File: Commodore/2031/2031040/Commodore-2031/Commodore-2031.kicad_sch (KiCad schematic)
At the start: 11 parts

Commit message: Capture sheet 3
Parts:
- removed UA3, UJ5, UL6: 74LS04, symbol 74xx:74LS04
- removed UB1: 74LS14, symbol 74xx:74LS14
- removed UC1: 7406, symbol 74xx:74LS06
- removed UK6: 74LS10, symbol 74xx:74LS10
- removed UL2: 74LS133, symbol 74xx:74LS133
- removed UM2: 74LS02, symbol 74xx:74LS02
- removed UM3: 74LS74, symbol 74xx:74LS74
- removed UM6: 74LS00, symbol 74xx:74LS00
- removed UP2: 74LS86, symbol 74xx:74LS86
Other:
- added sheet CPUMemoryPowerClock (Sheet3-CPUMemoryPowerClock.kicad_sch)

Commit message: Capture sheet 4
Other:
- added sheet StepperMotorRWAmplifier (Sheet4-StepperMotorRWAmplifier.kicad_sch)
- sheet CPUMemoryPowerClock ports: added 16MHZ; removed 16MHz

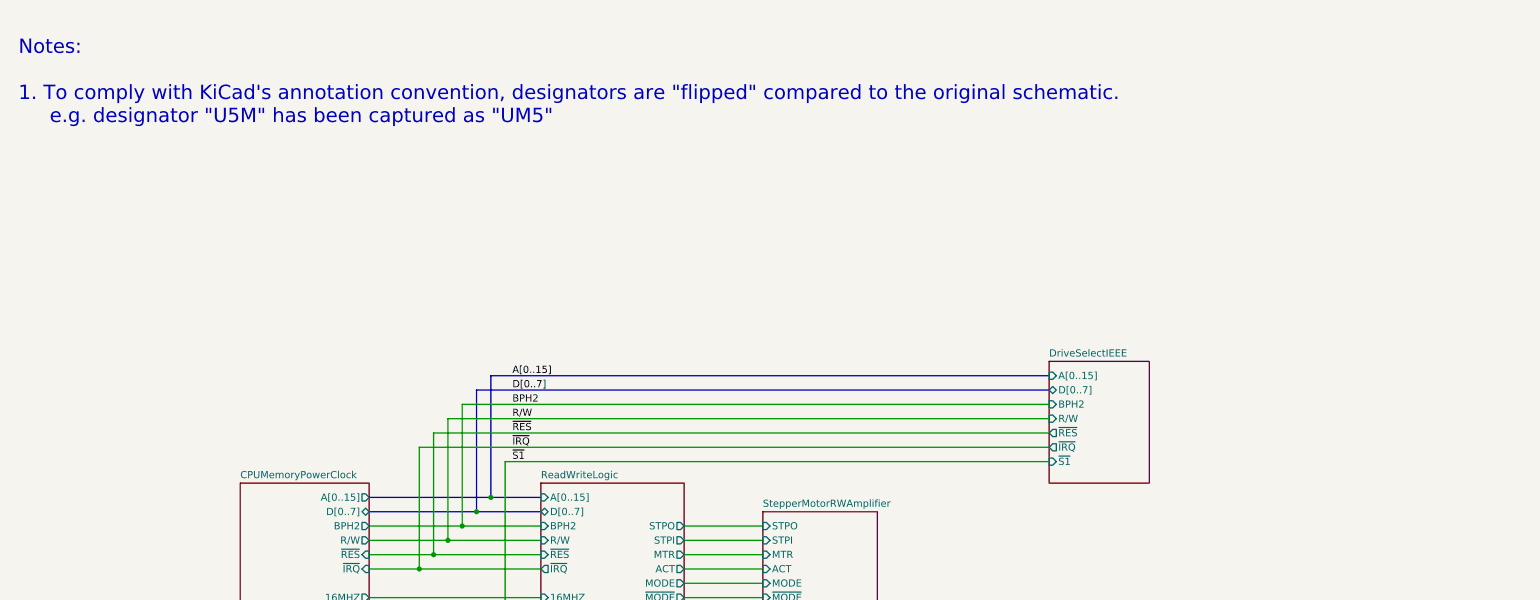
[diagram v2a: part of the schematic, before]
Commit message: Work towards ERC
- Add power flags
- Try to make sense of ground symbols
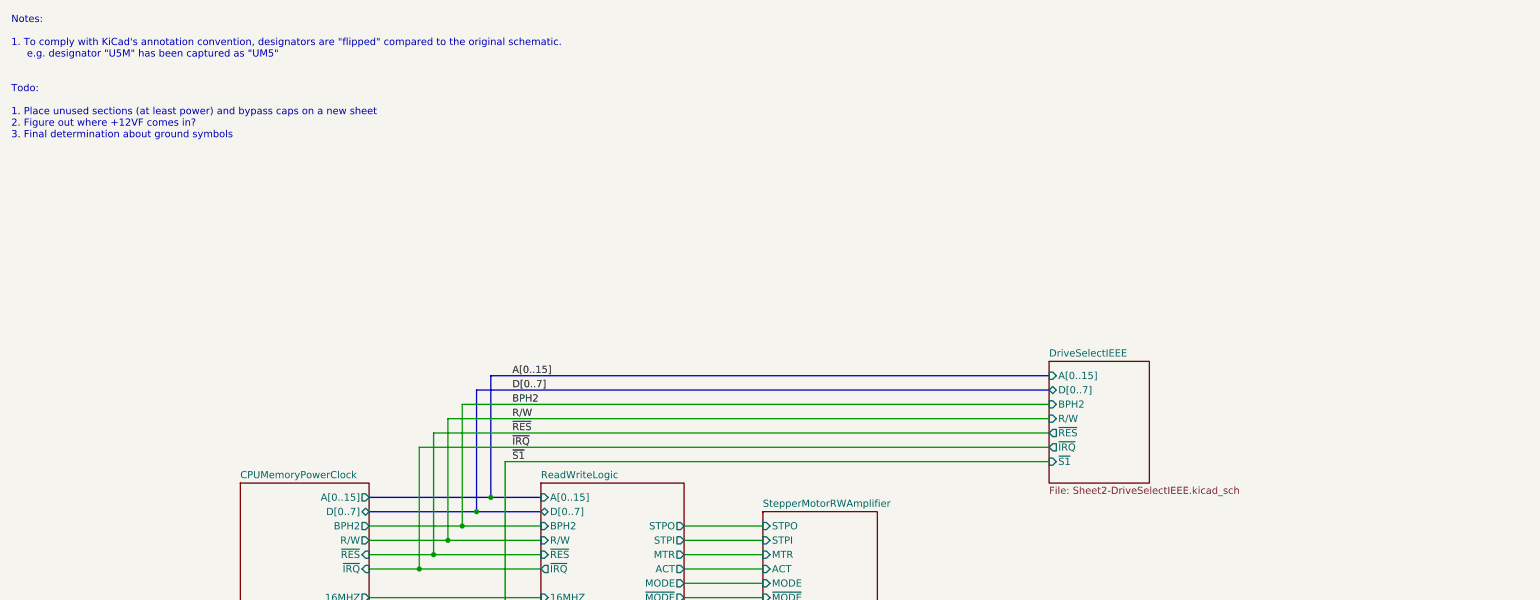
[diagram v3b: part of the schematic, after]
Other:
- note added: "Notes: 1. To comply with KiCad's annotation convention, designators are "flipped" compared to the original schematic. e.g. designator "U5M" has been captured as "UM5" Todo: 1. Place unused sections (at least power) and bypass caps on a new sheet 2. Figure out where +12VF comes in? 3. Final determination about ground symbols"
- note removed: "Notes: 1. To comply with KiCad's annotation convention, designators are "flipped" compared to the original schematic. e.g. designator "U5M" has been captured as "UM5""
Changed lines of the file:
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@@
     (stroke (width 0) (type default))
   )
-  (text "Notes:\n\n1. To comply with KiCad's annotation convention, designators are \"flipped\" compared to the original schematic.\n     e.g. designator \"U5M\" has been captured as \"UM5\""
-    (at 19.05 36.83 0)
-    (effects (font (size 2.54 2.54)) (justify left bottom))
+  (text "Notes:\n\n1. To comply with KiCad's annotation convention, designators are \"flipped\" compared to the original schematic.\n     e.g. designator \"U5M\" has been captured as \"UM5\"\n\n\nTodo:\n\n1. Place unused sections (at least power) and bypass caps on a new sheet\n2. Figure out where +12VF comes in?\n3. Final determination about ground symbols"
+    (at 17.78 39.37 0)
+    (effects (font (size 1.27 1.27)) (justify left bottom))
   )
   (label "A[0..15]" (at 106.68 81.28 0) (fields_autoplaced)
@@
     )
     (property "Sheetfile" "Sheet2-DriveSelectIEEE.kicad_sch" (at 201.93 100.9146 0)
-      (effects (font (size 1.27 1.27)) (justify left top) hide)
+      (effects (font (size 1.27 1.27)) (justify left top))
     )
     (pin "~{IRQ}" output (at 201.93 93.98 180)

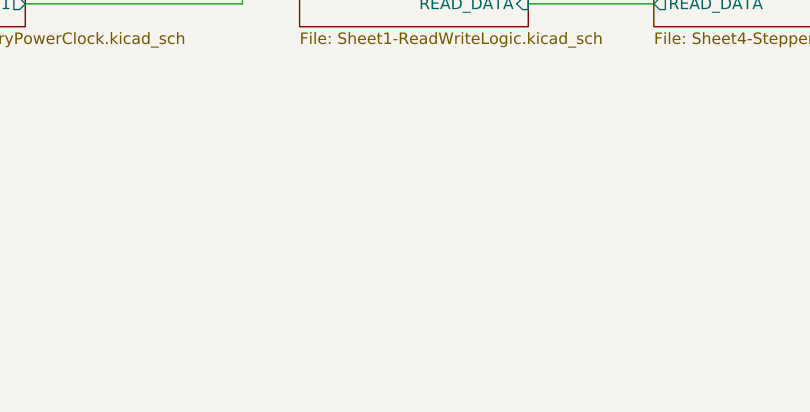
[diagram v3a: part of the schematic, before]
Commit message: Place capacitors and power units
Almost an error-free ERC!
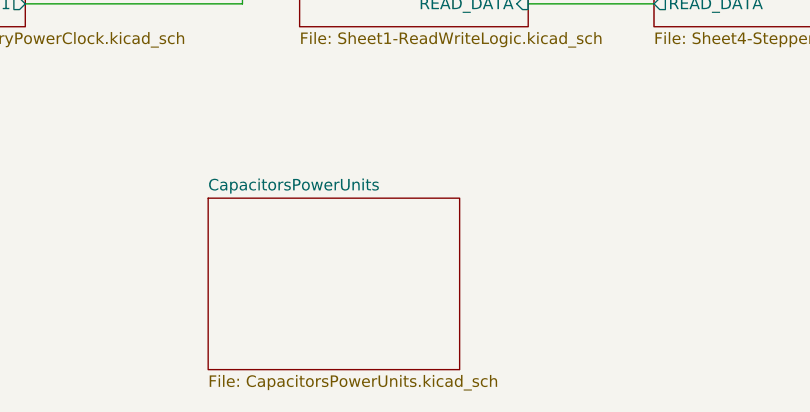
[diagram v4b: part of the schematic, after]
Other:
- added sheet CapacitorsPowerUnits (CapacitorsPowerUnits.kicad_sch)
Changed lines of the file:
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@@
+    )
+  )
+  (sheet (at 101.6 154.94) (size 27.94 19.05) (fields_autoplaced)
+    (stroke (width 0.1524) (type solid))
+    (fill (color 0 0 0 0.0000))
+    (property "Sheetname" "CapacitorsPowerUnits" (at 101.6 154.2284 0)
+      (effects (font (size 1.27 1.27)) (justify left bottom))
+    )
+    (property "Sheetfile" "CapacitorsPowerUnits.kicad_sch" (at 101.6 174.5746 0)
+      (effects (font (size 1.27 1.27)) (justify left top))
+    )
+    (instances
+      (project "Commodore-2031"
+        (path "/4559151c-aecb-4a2a-972f-dcb7dcb5a3dc" (page "6"))
+      )
     )
   )

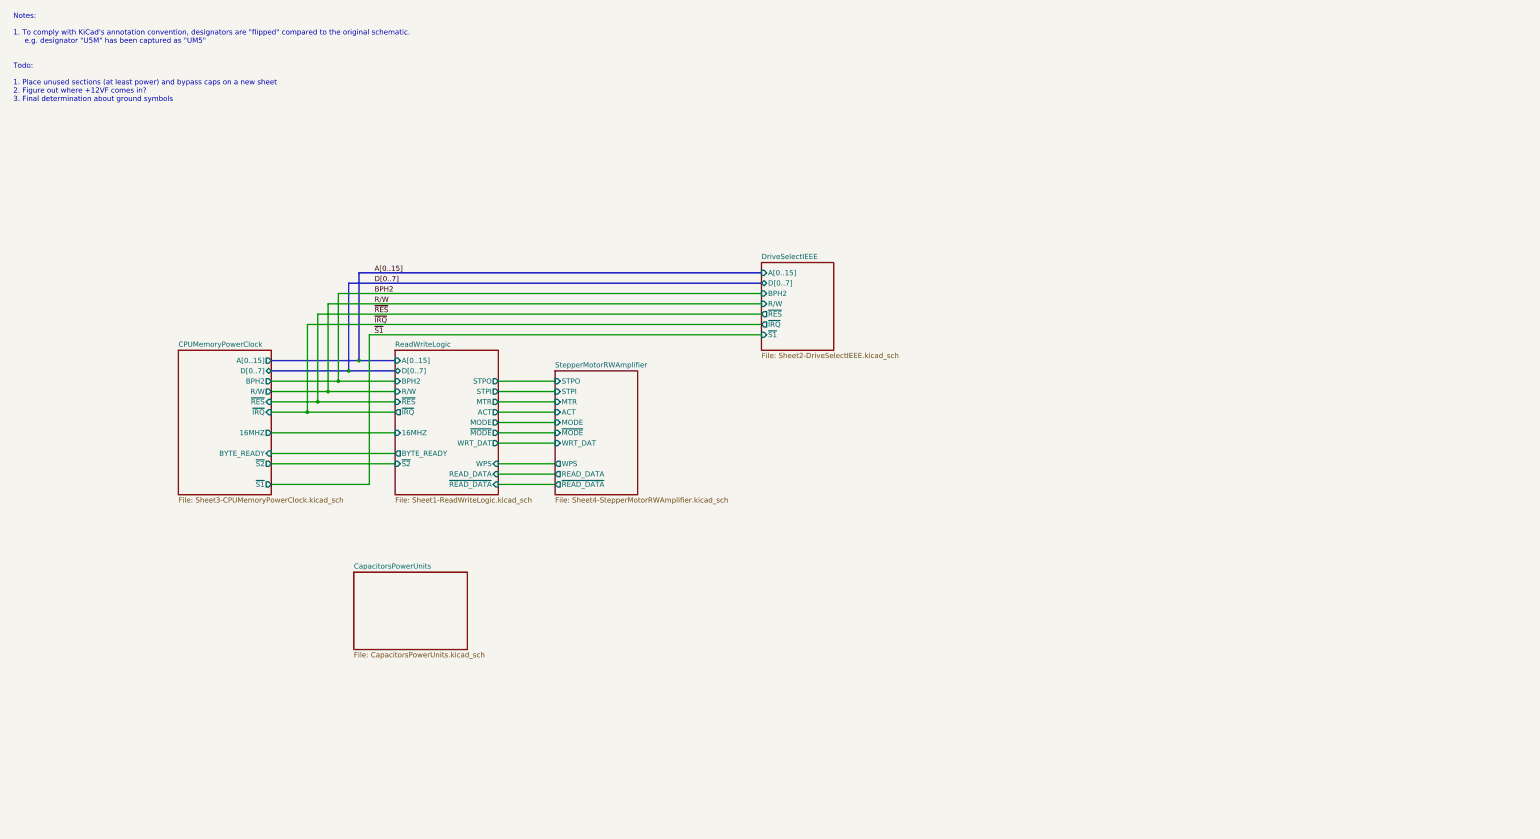
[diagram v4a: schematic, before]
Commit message: Resolve remaining ERC errors
... still lots of warnings tho.
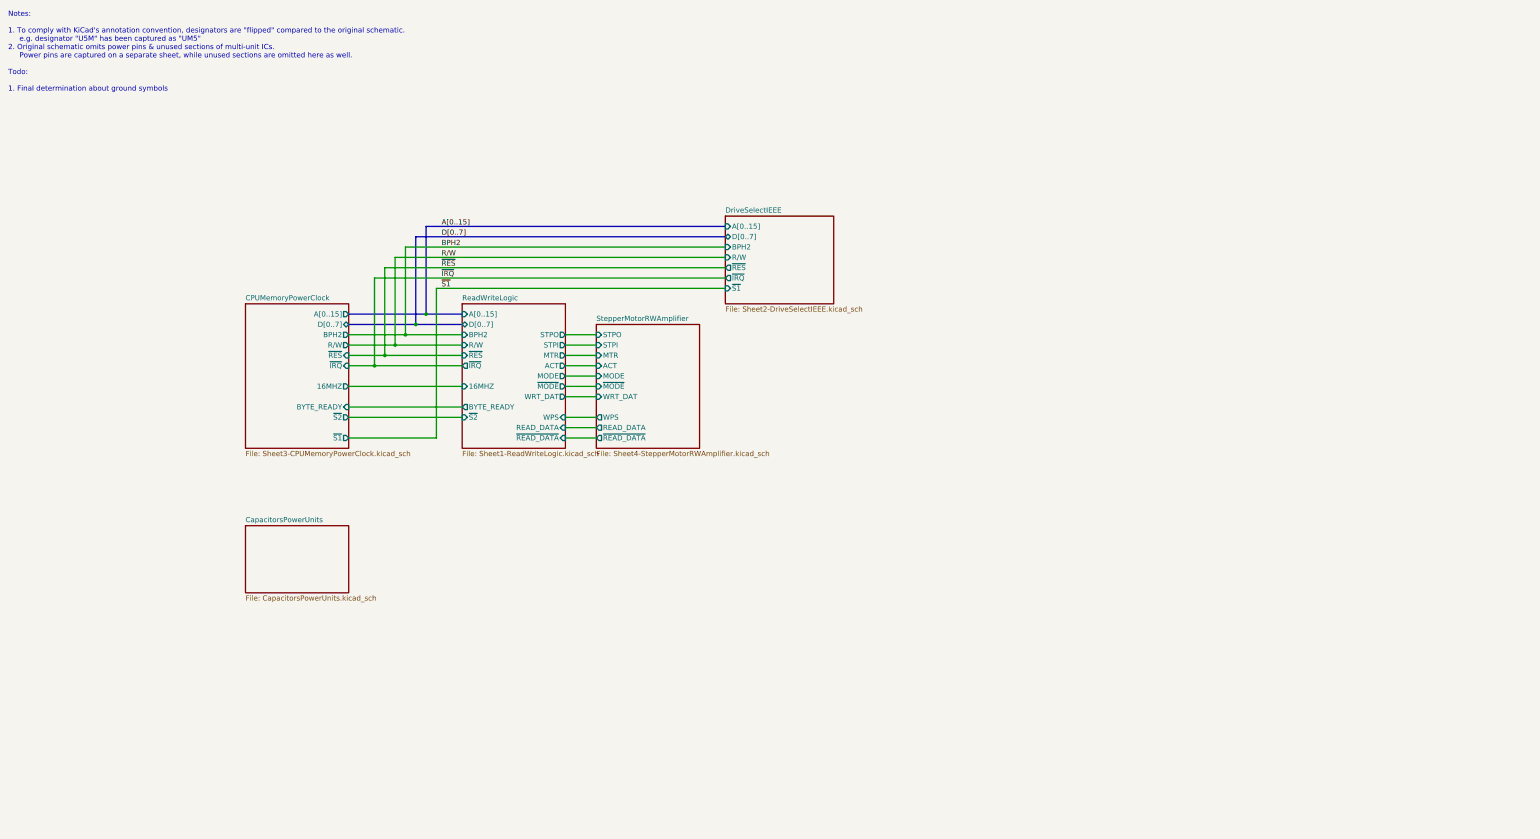
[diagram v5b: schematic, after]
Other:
- note added: "Notes: 1. To comply with KiCad's annotation convention, designators are "flipped" compared to the original schematic. e.g. designator "U5M" has been captured as "UM5" 2. Original schematic omits power pins & unused sections of multi-unit ICs. Power pins are captured on a separate sheet, while unused sections are omitted here as well. Todo: 1. Final determination about ground symbols"
- note removed: "Notes: 1. To comply with KiCad's annotation convention, designators are "flipped" compared to the original schematic. e.g. designator "U5M" has been captured as "UM5" Todo: 1. Place unused sections (at least power) and bypass caps on a new sheet 2. Figure out where +12VF comes in? 3. Final determination about ground symbols"

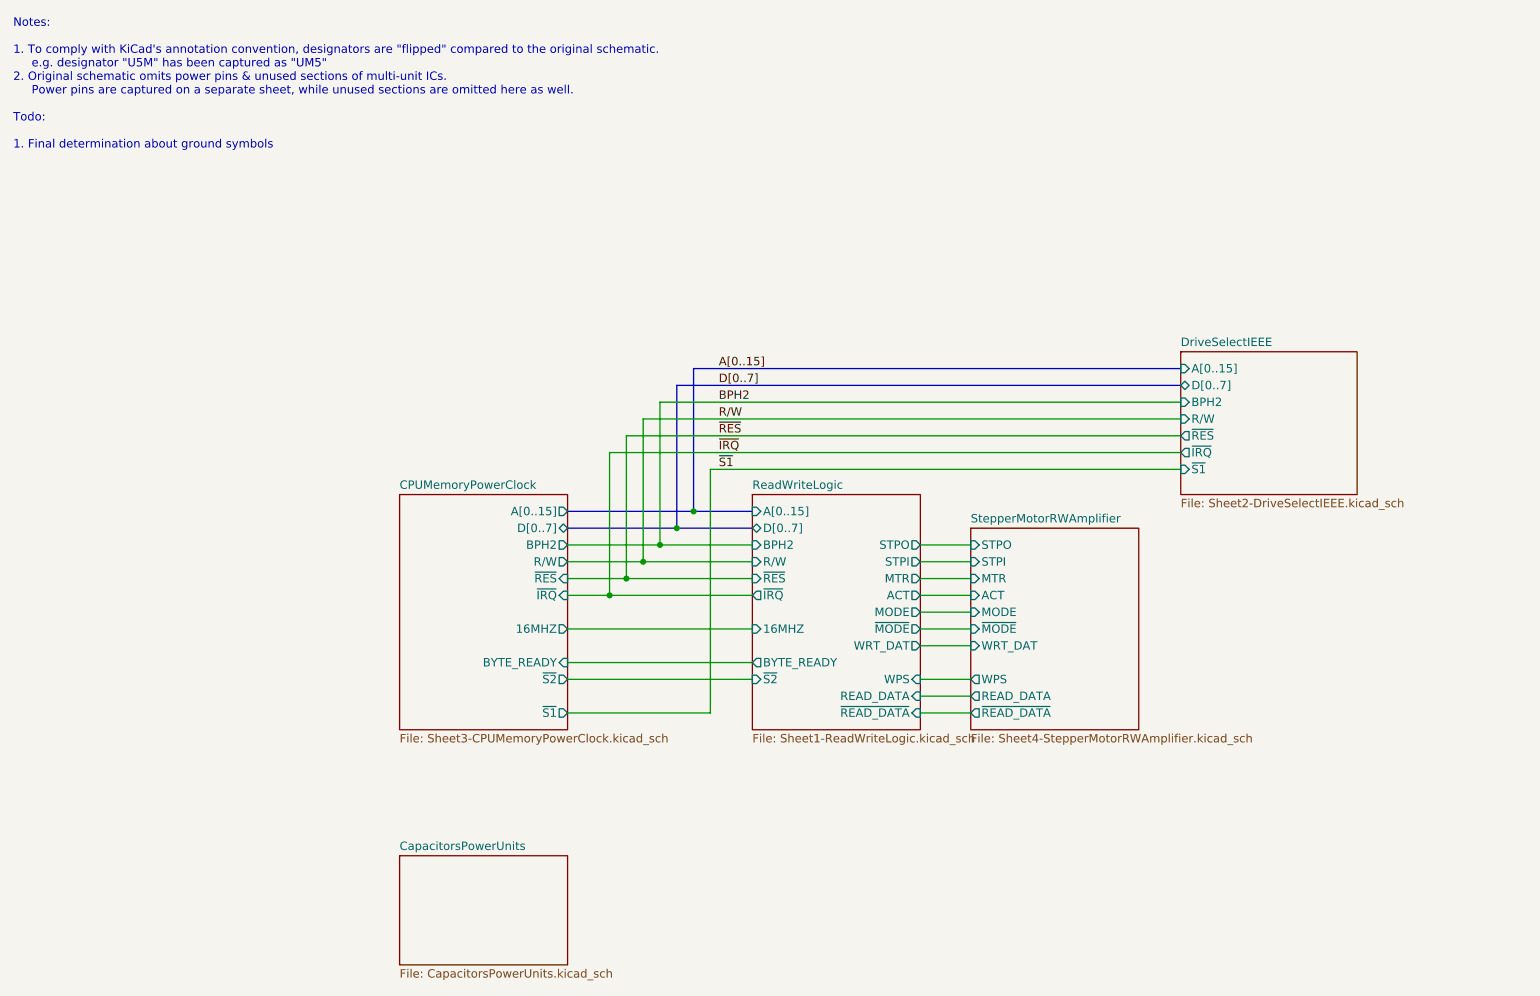
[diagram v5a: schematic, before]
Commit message: Verify schematic against parts list
A few discrepancies appear in original, these are noted in schematic.
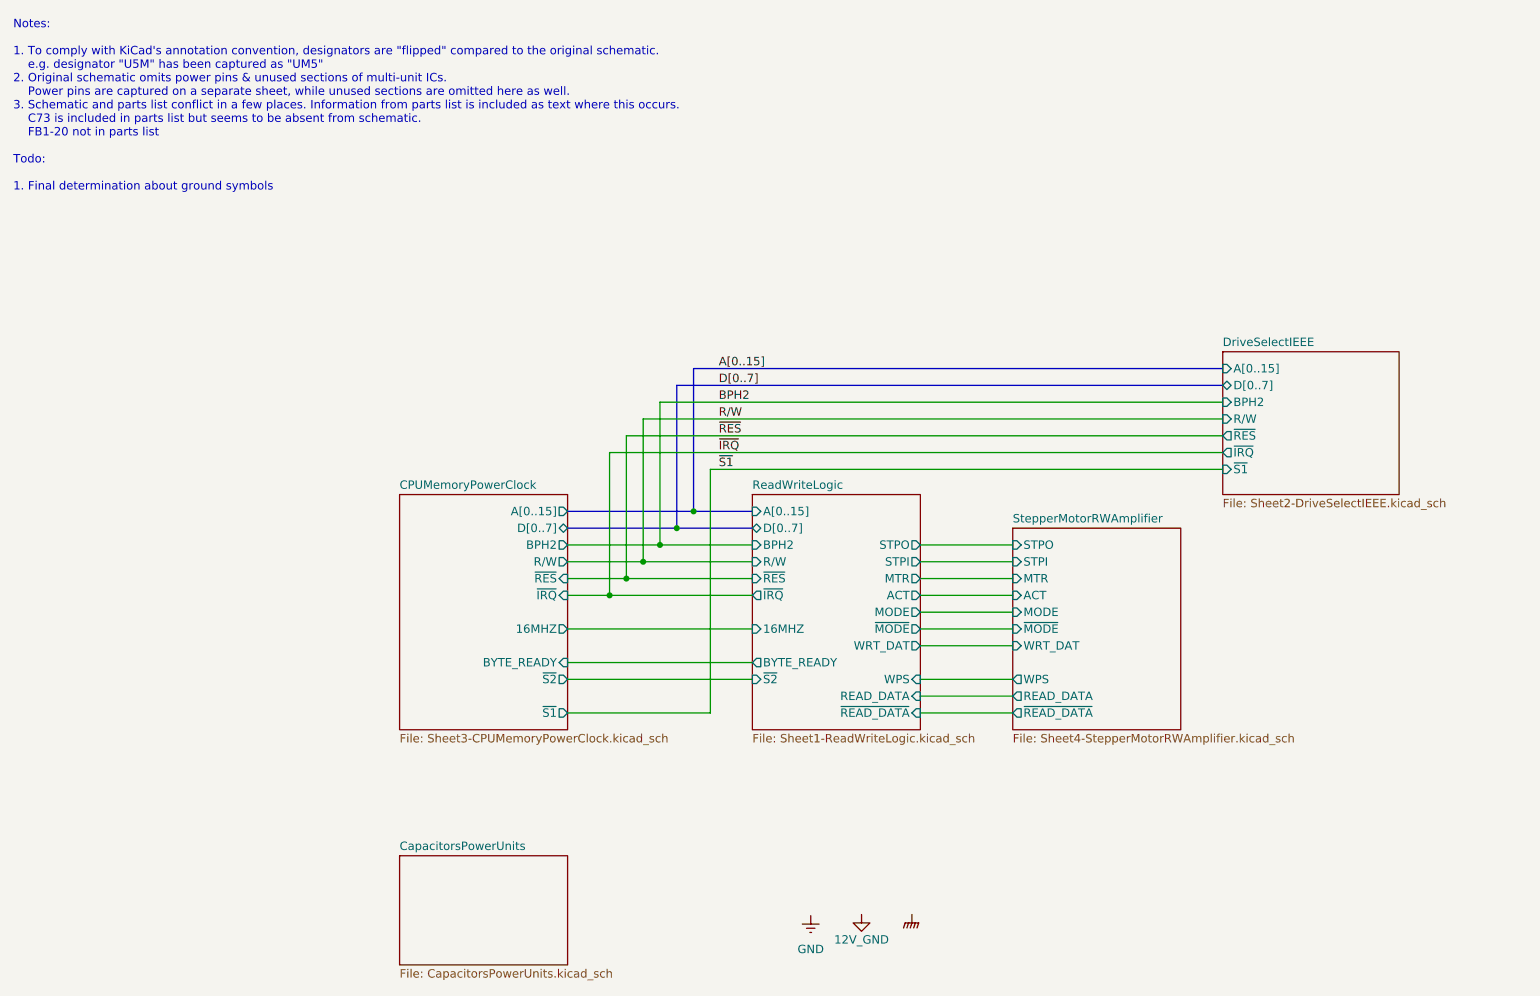
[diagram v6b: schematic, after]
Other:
- note added: "Notes: 1. To comply with KiCad's annotation convention, designators are "flipped" compared to the original schematic. e.g. designator "U5M" has been captured as "UM5" 2. Original schematic omits power pins & unused sections of multi-unit ICs. Power pins are captured on a separate sheet, while unused sections are omitted here as well. 3. Schematic and parts list conflict in a few places. Informati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"
- note removed: "Notes: 1. To comply with KiCad's annotation convention, designators are "flipped" compared to the original schematic. e.g. designator "U5M" has been captured as "UM5" 2. Original schematic omits power pins & unused sections of multi-unit ICs. Power pins are captured on a separate sheet, while unused sections are omitted here as well. Todo: 1. Final determination about ground symbols"
